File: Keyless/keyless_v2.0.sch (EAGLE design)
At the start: 43 parts, among them J1 AVR_SPI_PRG_6NS, U1 USD-SOCKET, X1 USB-SMD-NS, Y1 16MHz

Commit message: reasons
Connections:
- removed net 3.3V1: J1.2
- removed net B10: J1.4
- removed net B8: J1.3
- removed net B9: J1.1
- removed net RESET1: J1.5
- net 3.3V: now also J1.2
- net B1: now also J1.3
- net B2: now also J1.4
- net B3: now also J1.1
- net RESET: now also J1.5
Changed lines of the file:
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@@
 <wire x1="132.08" y1="119.38" x2="132.08" y2="121.92" width="0.1524" layer="91"/>
+</segment>
+<segment>
+<pinref part="J1" gate="G$1" pin="2"/>
+<wire x1="27.94" y1="15.24" x2="33.02" y2="15.24" width="0.1524" layer="91"/>
 </segment>
 </net>
@@
 <label x="127" y="104.14" size="1.778" layer="95" rot="MR0"/>
 </segment>
+<segment>
+<pinref part="J1" gate="G$1" pin="3"/>
+<wire x1="10.16" y1="12.7" x2="5.08" y2="12.7" width="0.1524" layer="91"/>
+</segment>
 </net>
 <net name="B3" class="0">
@@
 <label x="127" y="109.22" size="1.778" layer="95" rot="MR0"/>
 </segment>
+<segment>
+<pinref part="J1" gate="G$1" pin="1"/>
+<wire x1="10.16" y1="15.24" x2="5.08" y2="15.24" width="0.1524" layer="91"/>
+</segment>
 </net>
 <net name="B2" class="0">
@@
 <wire x1="127" y1="106.68" x2="119.38" y2="106.68" width="0.1524" layer="91"/>
 <label x="127" y="106.68" size="1.778" layer="95" rot="MR0"/>
+</segment>
+<segment>
+<pinref part="J1" gate="G$1" pin="4"/>
+<wire x1="27.94" y1="12.7" x2="33.02" y2="12.7" width="0.1524" layer="91"/>
 </segment>
 </net>
@@
 <wire x1="134.62" y1="10.16" x2="132.08" y2="10.16" width="0.1524" layer="91"/>
 </segment>
+<segment>
+<pinref part="J1" gate="G$1" pin="5"/>
+<wire x1="10.16" y1="10.16" x2="5.08" y2="10.16" width="0.1524" layer="91"/>
+</segment>
 </net>
 <net name="E2" class="0">
@@
 </segment>
 </net>
-<net name="B8" class="0">
-<segment>
-<pinref part="J1" gate="G$1" pin="3"/>
-<wire x1="10.16" y1="12.7" x2="5.08" y2="12.7" width="0.1524" layer="91"/>
-</segment>
-</net>
-<net name="B9" class="0">
-<segment>
-<pinref part="J1" gate="G$1" pin="1"/>
-<wire x1="10.16" y1="15.24" x2="5.08" y2="15.24" width="0.1524" layer="91"/>
-</segment>
-</net>
-<net name="B10" class="0">
-<segment>
-<pinref part="J1" gate="G$1" pin="4"/>
-<wire x1="27.94" y1="12.7" x2="33.02" y2="12.7" width="0.1524" layer="91"/>
-</segment>
-</net>
-<net name="RESET1" class="0">
-<segment>
-<pinref part="J1" gate="G$1" pin="5"/>
-<wire x1="10.16" y1="10.16" x2="5.08" y2="10.16" width="0.1524" layer="91"/>
-</segment>
-</net>
-<net name="3.3V1" class="0">
-<segment>
-<pinref part="J1" gate="G$1" pin="2"/>
-<wire x1="27.94" y1="15.24" x2="33.02" y2="15.24" width="0.1524" layer="91"/>
-</segment>
-</net>

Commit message: more wires!
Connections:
- removed net RAW: C19.1, JP2.2, SJ1.1, U$3.VCC
- net 5V: now also C19.1, JP2.2, SJ1.1, U$3.VCC
- net B7: now also JP1.7
- net D5: no longer JP1.7
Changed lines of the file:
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@@
 <pinref part="SUPPLY3" gate="G$1" pin="5V"/>
+</segment>
+<segment>
+<wire x1="15.24" y1="162.56" x2="15.24" y2="165.1" width="0.1524" layer="91"/>
+<wire x1="15.24" y1="165.1" x2="5.08" y2="165.1" width="0.1524" layer="91"/>
+<label x="5.08" y="165.1" size="1.778" layer="95"/>
+<pinref part="C19" gate="G$1" pin="1"/>
+<pinref part="U$3" gate="G$1" pin="VCC"/>
+<wire x1="25.4" y1="165.1" x2="15.24" y2="165.1" width="0.1524" layer="91"/>
+<junction x="15.24" y="165.1"/>
+</segment>
+<segment>
+<pinref part="SJ1" gate="1" pin="1"/>
+<wire x1="66.04" y1="177.8" x2="58.42" y2="177.8" width="0.1524" layer="91"/>
+<label x="58.42" y="177.8" size="1.778" layer="95"/>
+</segment>
+<segment>
+<wire x1="22.86" y1="175.26" x2="12.7" y2="175.26" width="0.1524" layer="91"/>
+<label x="22.86" y="175.26" size="1.778" layer="95" rot="MR0"/>
+<pinref part="JP2" gate="G$1" pin="2"/>
 </segment>
 </net>
@@
 <label x="231.14" y="38.1" size="1.778" layer="95"/>
 </segment>
+<segment>
+<pinref part="JP1" gate="G$1" pin="7"/>
+<wire x1="127" y1="116.84" x2="119.38" y2="116.84" width="0.1524" layer="91"/>
+<label x="127" y="116.84" size="1.778" layer="95" rot="MR0"/>
+</segment>
 </net>
 <net name="D6" class="0">
@@
 <label x="172.72" y="58.42" size="1.778" layer="95"/>
 </segment>
-<segment>
-<pinref part="JP1" gate="G$1" pin="7"/>
-<wire x1="127" y1="116.84" x2="119.38" y2="116.84" width="0.1524" layer="91"/>
-<label x="127" y="116.84" size="1.778" layer="95" rot="MR0"/>
-</segment>
 </net>
 <net name="N$14" class="0">
@@
 </segment>
 </net>
-<net name="RAW" class="1">
-<segment>
-<wire x1="15.24" y1="162.56" x2="15.24" y2="165.1" width="0.1524" layer="91"/>
-<wire x1="15.24" y1="165.1" x2="5.08" y2="165.1" width="0.1524" layer="91"/>
-<label x="5.08" y="165.1" size="1.778" layer="95"/>
-<pinref part="C19" gate="G$1" pin="1"/>
-<pinref part="U$3" gate="G$1" pin="VCC"/>
-<wire x1="25.4" y1="165.1" x2="15.24" y2="165.1" width="0.1524" layer="91"/>
-<junction x="15.24" y="165.1"/>
-</segment>
-<segment>
-<pinref part="SJ1" gate="1" pin="1"/>
-<wire x1="66.04" y1="177.8" x2="58.42" y2="177.8" width="0.1524" layer="91"/>
-<label x="58.42" y="177.8" size="1.778" layer="95"/>
-</segment>
-<segment>
-<wire x1="22.86" y1="175.26" x2="12.7" y2="175.26" width="0.1524" layer="91"/>
-<label x="22.86" y="175.26" size="1.778" layer="95" rot="MR0"/>
-<pinref part="JP2" gate="G$1" pin="2"/>
-</segment>
-</net>

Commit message: more routing!
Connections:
- removed net N$20: U1.CD1
- removed net N$21: U1.CD2
- net F4: now also U1.CD1
- net GND: now also U1.CD2
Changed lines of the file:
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@@
 <part name="GND24" library="SparkFun" deviceset="GND" device=""/>
 <part name="JP3" library="SparkFun-Connectors" deviceset="M08" device="1X08"/>
+<part name="GND26" library="SparkFun-Aesthetics" deviceset="GND" device=""/>
 </parts>
 <sheets>
@@
 <instance part="GND24" gate="1" x="116.84" y="50.8"/>
 <instance part="JP3" gate="G$1" x="76.2" y="66.04"/>
+<instance part="GND26" gate="1" x="99.06" y="93.98"/>
 </instances>
 <busses>
@@
 <pinref part="GND24" gate="1" pin="GND"/>
 </segment>
+<segment>
+<pinref part="U1" gate="G$1" pin="CD2"/>
+<wire x1="99.06" y1="96.52" x2="91.44" y2="96.52" width="0.1524" layer="91"/>
+<pinref part="GND26" gate="1" pin="GND"/>
+</segment>
 </net>
 <net name="5V" class="0">
@@
 <label x="231.14" y="91.44" size="1.778" layer="95"/>
 </segment>
+<segment>
+<pinref part="U1" gate="G$1" pin="CD1"/>
+<wire x1="99.06" y1="99.06" x2="91.44" y2="99.06" width="0.1524" layer="91"/>
+<label x="99.06" y="99.06" size="1.778" layer="95" rot="MR0"/>
+</segment>
 </net>
 <net name="F5" class="0">
@@
 </segment>
 </net>
-<net name="N$20" class="0">
-<segment>
-<pinref part="U1" gate="G$1" pin="CD1"/>
-<wire x1="99.06" y1="99.06" x2="91.44" y2="99.06" width="0.1524" layer="91"/>
-</segment>
-</net>
-<net name="N$21" class="0">
-<segment>
-<pinref part="U1" gate="G$1" pin="CD2"/>
-<wire x1="99.06" y1="96.52" x2="91.44" y2="96.52" width="0.1524" layer="91"/>
-</segment>
-</net>

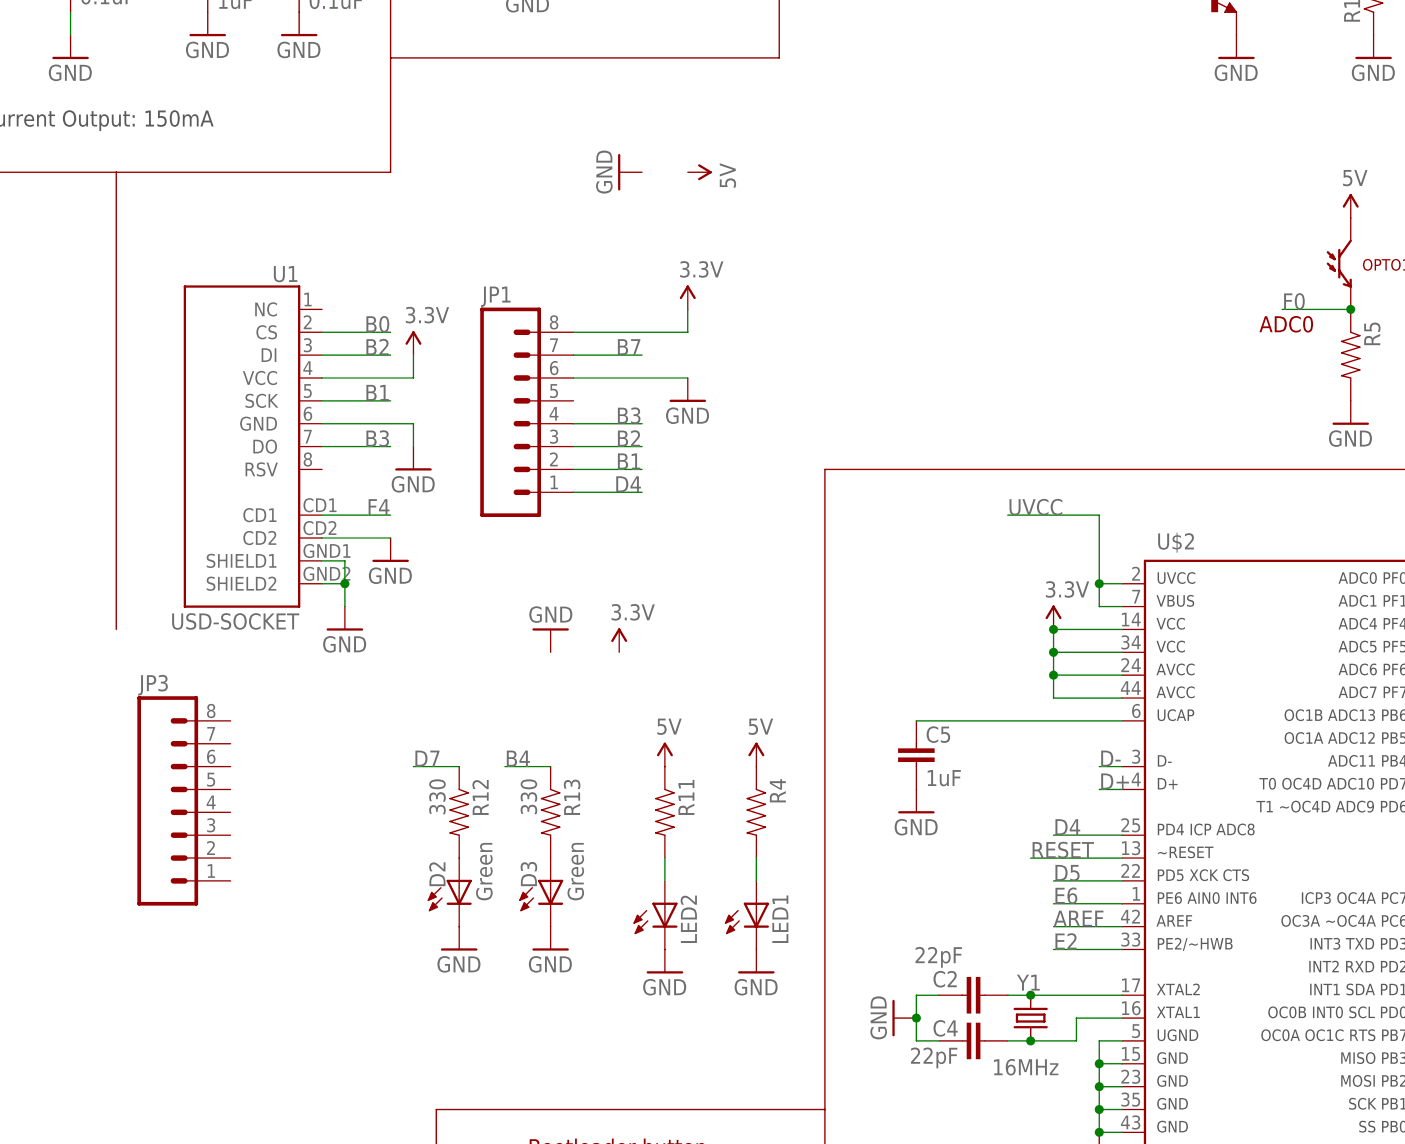
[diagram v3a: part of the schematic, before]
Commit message: added pin breakouts
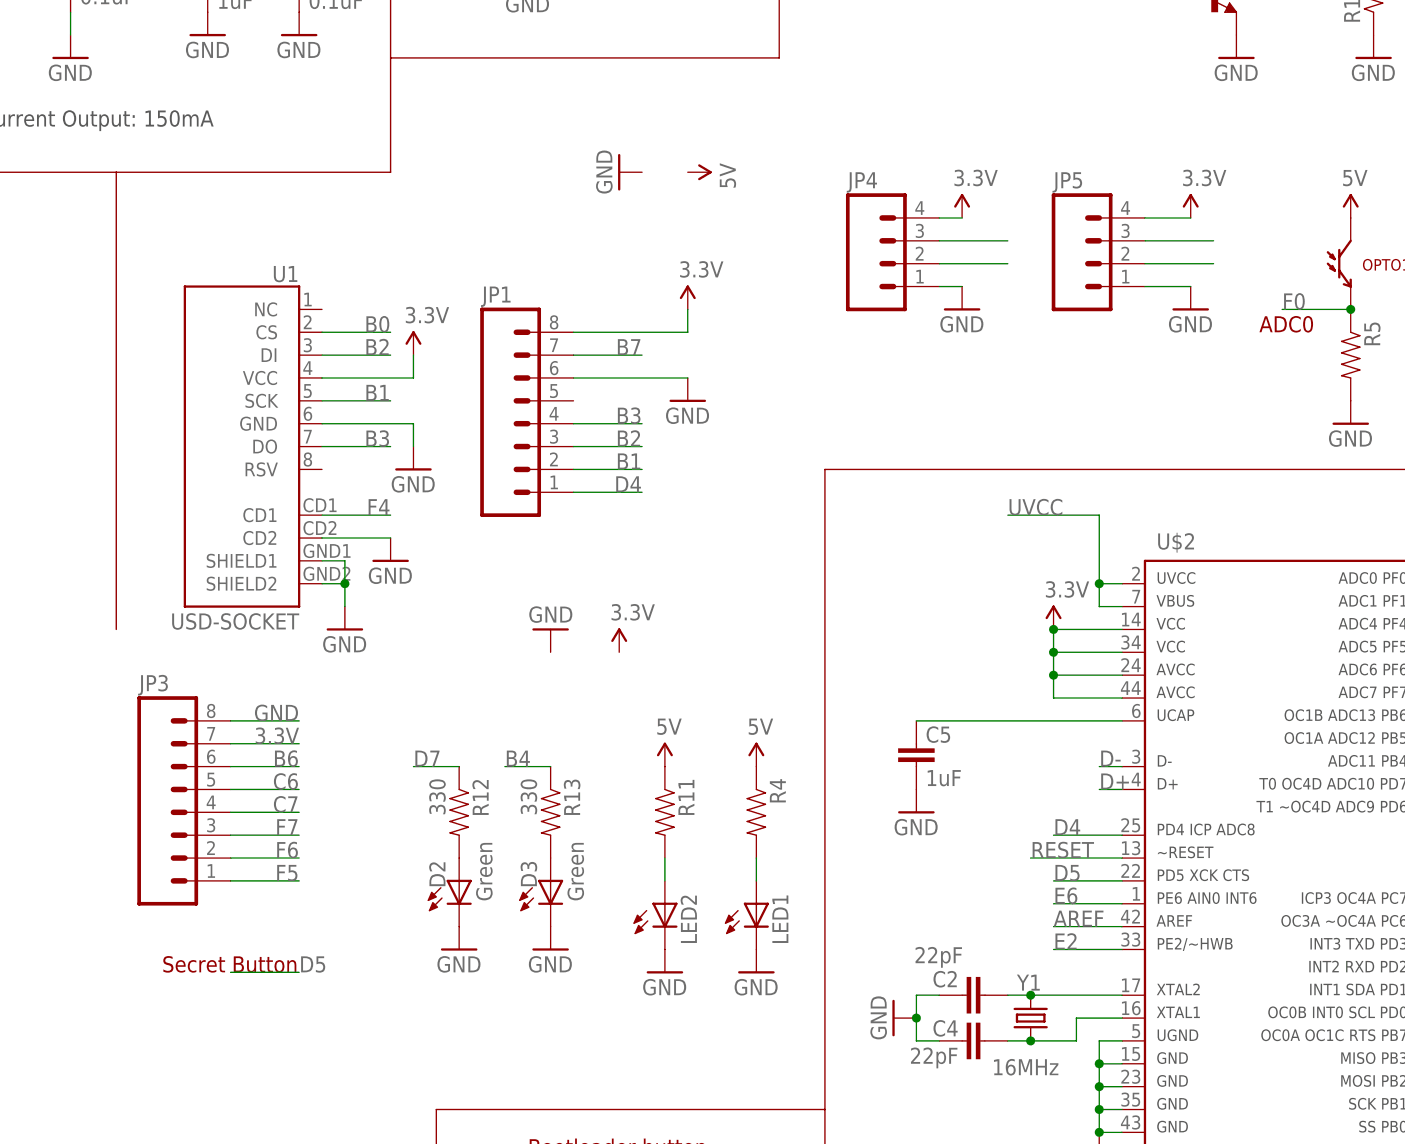
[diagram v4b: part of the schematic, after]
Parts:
- added JP4, JP5: (no value), SparkFun-Connectors:M04PTH
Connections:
- net 3.3V: now also JP3.7, JP4.4, JP5.4
- net B6: now also JP3.6
- net C6: now also JP3.5
- net C7: now also JP3.4
- net D0: now also JP5.2
- net D1: now also JP5.3
- net D2: now also JP4.2
- net D3: now also JP4.3
- net F5: now also JP3.1
- net F6: now also JP3.2
- net F7: now also JP3.3
- net GND: now also JP3.8, JP4.1, JP5.1
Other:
- note added: "Secret Button"
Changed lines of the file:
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@@
 <layer number="91" name="Nets" color="2" fill="1" visible="yes" active="yes"/>
 <layer number="92" name="Busses" color="1" fill="1" visible="yes" active="yes"/>
-<layer number="93" name="Pins" color="2" fill="1" visible="no" active="yes"/>
+<layer number="93" name="Pins" color="2" fill="1" visible="yes" active="yes"/>
 <layer number="94" name="Symbols" color="4" fill="1" visible="yes" active="yes"/>
 <layer number="95" name="Names" color="7" fill="1" visible="yes" active="yes"/>
@@
 <part name="JP3" library="SparkFun-Connectors" deviceset="M08" device="1X08"/>
 <part name="GND26" library="SparkFun-Aesthetics" deviceset="GND" device=""/>
+<part name="JP4" library="SparkFun-Connectors" deviceset="M04" device="PTH"/>
+<part name="JP5" library="SparkFun-Connectors" deviceset="M04" device="PTH"/>
+<part name="P+5" library="SparkFun" deviceset="3.3V" device=""/>
+<part name="P+6" library="SparkFun" deviceset="3.3V" device=""/>
+<part name="GND27" library="SparkFun" deviceset="GND" device=""/>
+<part name="GND28" library="SparkFun" deviceset="GND" device=""/>
 </parts>
 <sheets>
@@
 <wire x1="147.32" y1="33.02" x2="104.14" y2="33.02" width="0.1524" layer="94"/>
 <wire x1="104.14" y1="33.02" x2="104.14" y2="0" width="0.1524" layer="94"/>
+<text x="73.66" y="48.26" size="1.778" layer="94">Secret Button</text>
 </plain>
 <instances>
@@
 <instance part="JP3" gate="G$1" x="76.2" y="66.04"/>
 <instance part="GND26" gate="1" x="99.06" y="93.98"/>
+<instance part="JP4" gate="G$1" x="154.94" y="127"/>
+<instance part="JP5" gate="G$1" x="177.8" y="127"/>
+<instance part="P+5" gate="G$1" x="162.56" y="132.08"/>
+<instance part="P+6" gate="G$1" x="187.96" y="132.08"/>
+<instance part="GND27" gate="1" x="162.56" y="121.92"/>
+<instance part="GND28" gate="1" x="187.96" y="121.92"/>
 </instances>
 <busses>
@@
 <pinref part="GND26" gate="1" pin="GND"/>
 </segment>
+<segment>
+<wire x1="88.9" y1="76.2" x2="81.28" y2="76.2" width="0.1524" layer="91"/>
+<label x="88.9" y="76.2" size="1.778" layer="95" rot="MR0"/>
+<pinref part="JP3" gate="G$1" pin="8"/>
+</segment>
+<segment>
+<pinref part="GND27" gate="1" pin="GND"/>
+<pinref part="JP4" gate="G$1" pin="1"/>
+<wire x1="162.56" y1="124.46" x2="160.02" y2="124.46" width="0.1524" layer="91"/>
+</segment>
+<segment>
+<pinref part="JP5" gate="G$1" pin="1"/>
+<pinref part="GND28" gate="1" pin="GND"/>
+<wire x1="182.88" y1="124.46" x2="187.96" y2="124.46" width="0.1524" layer="91"/>
+</segment>
 </net>
 <net name="5V" class="0">
@@
 <wire x1="27.94" y1="15.24" x2="33.02" y2="15.24" width="0.1524" layer="91"/>
 </segment>
+<segment>
+<wire x1="88.9" y1="73.66" x2="81.28" y2="73.66" width="0.1524" layer="91"/>
+<label x="88.9" y="73.66" size="1.778" layer="95" rot="MR0"/>
+<pinref part="JP3" gate="G$1" pin="7"/>
+</segment>
+<segment>
+<pinref part="P+5" gate="G$1" pin="3.3V"/>
+<pinref part="JP4" gate="G$1" pin="4"/>
+<wire x1="162.56" y1="132.08" x2="160.02" y2="132.08" width="0.1524" layer="91"/>
+</segment>
+<segment>
+<pinref part="P+6" gate="G$1" pin="3.3V"/>
+<pinref part="JP5" gate="G$1" pin="4"/>
+<wire x1="187.96" y1="132.08" x2="182.88" y2="132.08" width="0.1524" layer="91"/>
+</segment>
 </net>
 <net name="AREF" class="0">
@@
 <label x="231.14" y="88.9" size="1.778" layer="95"/>
 </segment>
+<segment>
+<wire x1="81.28" y1="58.42" x2="88.9" y2="58.42" width="0.1524" layer="91"/>
+<label x="88.9" y="58.42" size="1.778" layer="95" rot="MR0"/>
+<pinref part="JP3" gate="G$1" pin="1"/>
+</segment>
 </net>
 <net name="F6" class="0">
@@
 <label x="231.14" y="86.36" size="1.778" layer="95"/>
 </segment>
+<segment>
+<wire x1="81.28" y1="60.96" x2="88.9" y2="60.96" width="0.1524" layer="91"/>
+<label x="88.9" y="60.96" size="1.778" layer="95" rot="MR0"/>
+<pinref part="JP3" gate="G$1" pin="2"/>
+</segment>
 </net>
 <net name="F7" class="0">
@@
 <label x="231.14" y="83.82" size="1.778" layer="95"/>
 </segment>
+<segment>
+<wire x1="81.28" y1="63.5" x2="88.9" y2="63.5" width="0.1524" layer="91"/>
+<label x="88.9" y="63.5" size="1.778" layer="95" rot="MR0"/>
+<pinref part="JP3" gate="G$1" pin="3"/>
+</segment>
 </net>
 <net name="D2" class="0">
@@
 <label x="231.14" y="45.72" size="1.778" layer="95"/>
 </segment>
+<segment>
+<wire x1="160.02" y1="127" x2="167.64" y2="127" width="0.1524" layer="91"/>
+<pinref part="JP4" gate="G$1" pin="2"/>
+</segment>
 </net>
 <net name="D3" class="0">
@@
 <label x="231.14" y="48.26" size="1.778" layer="95"/>
 </segment>
+<segment>
+<wire x1="160.02" y1="129.54" x2="167.64" y2="129.54" width="0.1524" layer="91"/>
+<pinref part="JP4" gate="G$1" pin="3"/>
+</segment>
 </net>
 <net name="D4" class="0">
@@
 <label x="231.14" y="50.8" size="1.778" layer="95"/>
 </segment>
+<segment>
+<wire x1="81.28" y1="68.58" x2="88.9" y2="68.58" width="0.1524" layer="91"/>
+<label x="88.9" y="68.58" size="1.778" layer="95" rot="MR0"/>
+<pinref part="JP3" gate="G$1" pin="5"/>
+</segment>
 </net>
 <net name="D7" class="0">
@@
 <label x="220.98" y="76.2" size="1.778" layer="95"/>
 <label x="231.14" y="81.28" size="1.778" layer="95"/>
+</segment>
+<segment>
+<wire x1="81.28" y1="71.12" x2="88.9" y2="71.12" width="0.1524" layer="91"/>
+<label x="88.9" y="71.12" size="1.778" layer="95" rot="MR0"/>
+<pinref part="JP3" gate="G$1" pin="6"/>
 </segment>
 </net>
@@
 <label x="231.14" y="53.34" size="1.778" layer="95"/>
 </segment>
+<segment>
+<wire x1="81.28" y1="66.04" x2="88.9" y2="66.04" width="0.1524" layer="91"/>
+<label x="88.9" y="66.04" size="1.778" layer="95" rot="MR0"/>
+<pinref part="JP3" gate="G$1" pin="4"/>
+</segment>
 </net>
 <net name="B5" class="0">
@@
 <label x="172.72" y="58.42" size="1.778" layer="95"/>
 </segment>
+<segment>
+<wire x1="88.9" y1="48.26" x2="81.28" y2="48.26" width="0.1524" layer="91"/>
+<label x="88.9" y="48.26" size="1.778" layer="95"/>
+</segment>
 </net>
 <net name="N$14" class="0">
@@
 <label x="231.14" y="43.18" size="1.778" layer="95"/>
 </segment>
+<segment>
+<wire x1="182.88" y1="129.54" x2="190.5" y2="129.54" width="0.1524" layer="91"/>
+<pinref part="JP5" gate="G$1" pin="3"/>
+</segment>
 </net>
 <net name="D0" class="0">
@@
 <label x="231.14" y="40.64" size="1.778" layer="95"/>
 </segment>
-</net>
+<segment>
+<wire x1="182.88" y1="127" x2="190.5" y2="127" width="0.1524" layer="91"/>
+<pinref part="JP5" gate="G$1" pin="2"/>
+</segment>
+</net>
